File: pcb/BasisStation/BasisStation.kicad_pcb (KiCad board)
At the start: 2 copper layers, 160 x 135 mm, 80 parts, among them J1 12401598E4-2A, J6 61200621621, Q1 BC337, Q2 BC337, Q3 BC337, Q4 BC337, T1 7499011121A, U1 D3V3XA4B10LP, U6 ESP32-S3-WROOM-1U-N16R8, U7 W5500, Y1 25 MHz

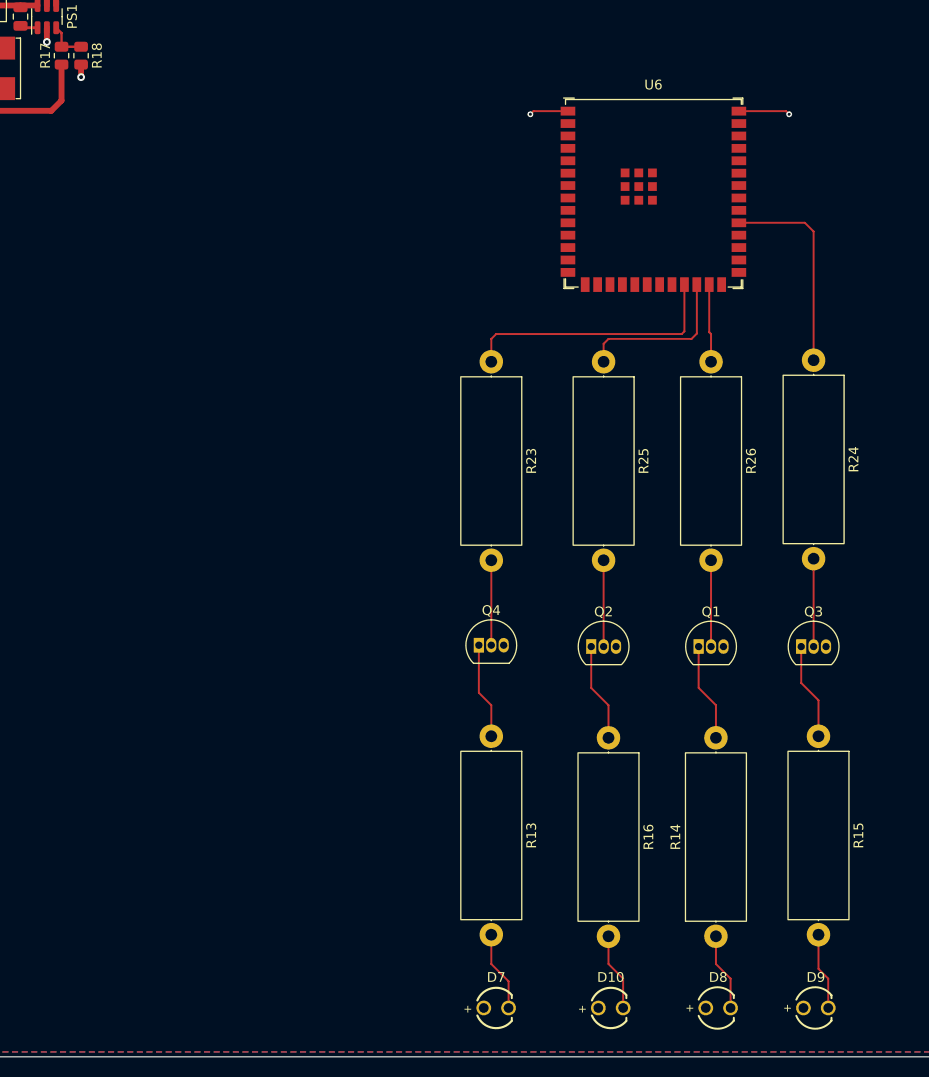
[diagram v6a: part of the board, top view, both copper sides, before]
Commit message: v0.00.001 feat(SHBS-21): +3V3 zu U6 und LED-Anoden geroutet, Task 0047 abgeschlossen
+3V3 auf F.Cu (0,6 mm) vom Wandler zu U6.2 und über U6 hinweg rechts
herum zur Sammelleitung unter D7-D10. Linke Seite von U6 bleibt für USB,
EN und ETH-SPI frei. Restpunkte (Aufweiten VBUS/+5V, DRC-Ausschlüsse
J_PWR1) in Task 0048 ausgelagert. hardware.md um Layout-Stand ergänzt.

Co-Authored-By: Claude Opus 5.5 <noreply@anthropic.com>
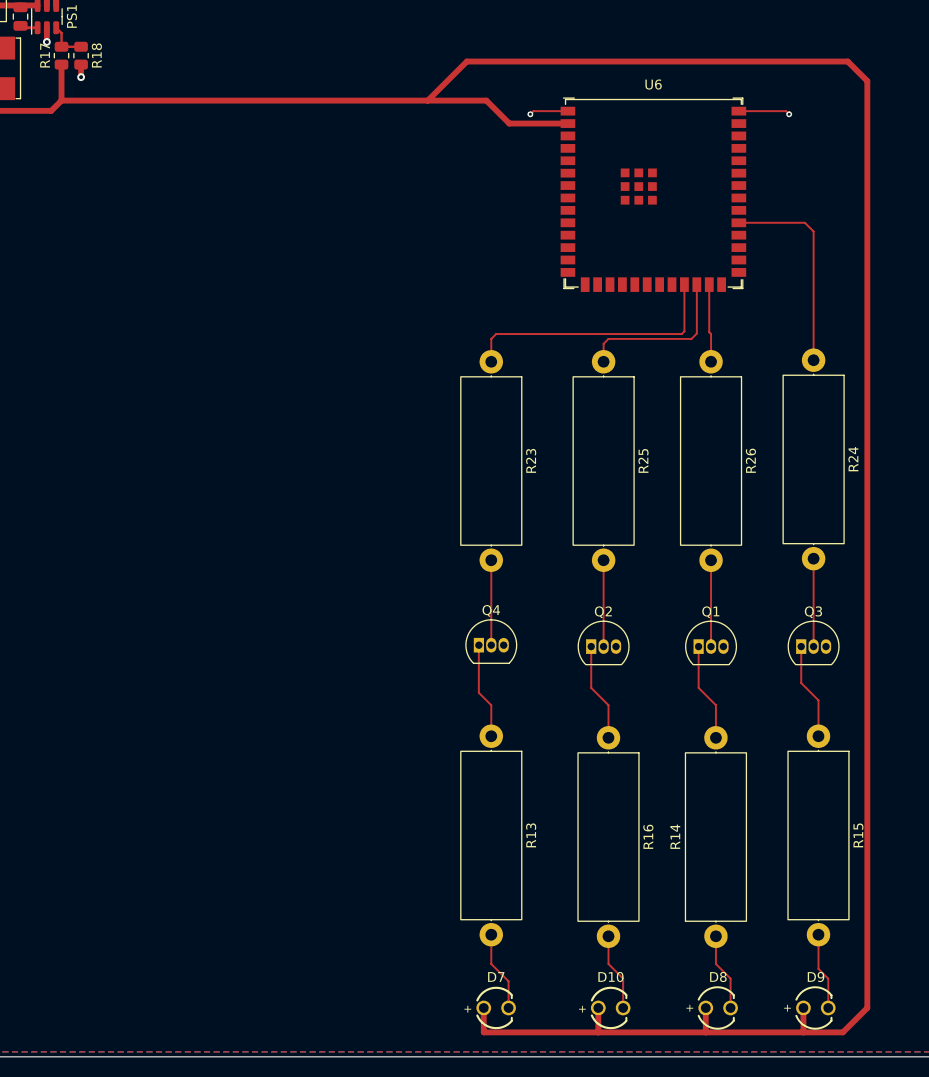
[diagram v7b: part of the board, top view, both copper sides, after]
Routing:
- net +3V3: track 13.7 -> 259.2 mm
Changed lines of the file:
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@@
+	)
+	(segment
+		(start 143.46 157.5)
+		(end 143.46 155)
+		(width 0.6)
+		(layer "F.Cu")
+		(net 2)
+	)
+	(segment
+		(start 67.5 62.1)
+		(end 105 62.1)
+		(width 0.6)
+		(layer "F.Cu")
+		(net 2)
+	)
+	(segment
+		(start 147.5 157.5)
+		(end 143.46 157.5)
+		(width 0.6)
+		(layer "F.Cu")
+		(net 2)
+	)
+	(segment
+		(start 122.46 157.5)
+		(end 122.46 155)
+		(width 0.6)
+		(layer "F.Cu")
+		(net 2)
+	)
+	(segment
+		(start 150 155)
+		(end 147.5 157.5)
+		(width 0.6)
+		(layer "F.Cu")
+		(net 2)
+	)
+	(segment
+		(start 105 62.1)
+		(end 111 62.1)
+		(width 0.6)
+		(layer "F.Cu")
+		(net 2)
+	)
+	(segment
+		(start 110.73 157.5)
+		(end 122.46 157.5)
+		(width 0.6)
+		(layer "F.Cu")
+		(net 2)
+	)
+	(segment
+		(start 111 62.1)
+		(end 113.35 64.45)
+		(width 0.6)
+		(layer "F.Cu")
+		(net 2)
+	)
+	(segment
+		(start 105 62.1)
+		(end 109 58.1)
+		(width 0.6)
+		(layer "F.Cu")
+		(net 2)
+	)
+	(segment
+		(start 113.35 64.45)
+		(end 119.35 64.45)
+		(width 0.6)
+		(layer "F.Cu")
+		(net 2)
+	)
+	(segment
+		(start 122.46 157.5)
+		(end 133.46 157.5)
+		(width 0.6)
+		(layer "F.Cu")
+		(net 2)
+	)
+	(segment
+		(start 110.73 157.5)
+		(end 110.73 155)
+		(width 0.6)
+		(layer "F.Cu")
+		(net 2)
+	)
+	(segment
+		(start 133.46 157.5)
+		(end 143.46 157.5)
+		(width 0.6)
+		(layer "F.Cu")
+		(net 2)
+	)
+	(segment
+		(start 150 60.1)
+		(end 150 155)
+		(width 0.6)
+		(layer "F.Cu")
+		(net 2)
+	)
+	(segment
+		(start 133.46 157.5)
+		(end 133.46 155)
+		(width 0.6)
+		(layer "F.Cu")
+		(net 2)
+	)
+	(segment
+		(start 109 58.1)
+		(end 148 58.1)
+		(width 0.6)
+		(layer "F.Cu")
+		(net 2)
 	)
 	(segment
@@
 		(width 0.6)
 		(layer "F.Cu")
+		(net 2)
+	)
+	(segment
+		(start 148 58.1)
+		(end 150 60.1)
+		(width 0.6)
+		(layer "F.Cu")
